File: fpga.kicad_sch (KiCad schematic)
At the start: 62 parts, among them IC4 XC3S250E-4VQG100C

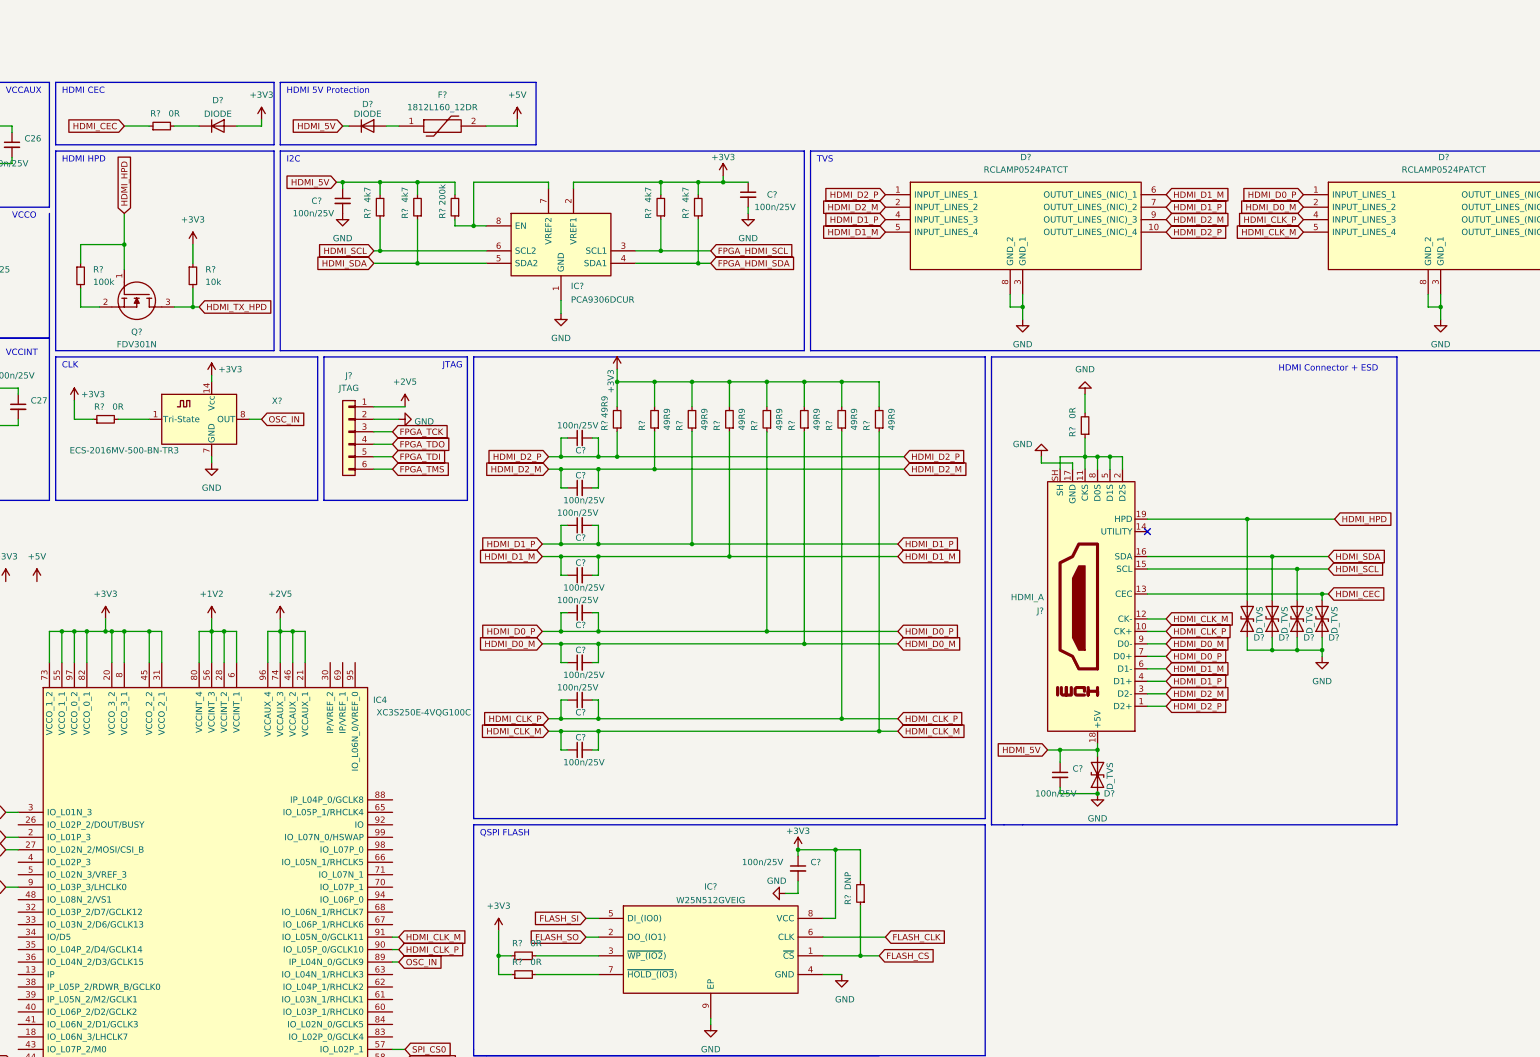
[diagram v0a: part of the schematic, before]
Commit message: update footprints for fpga
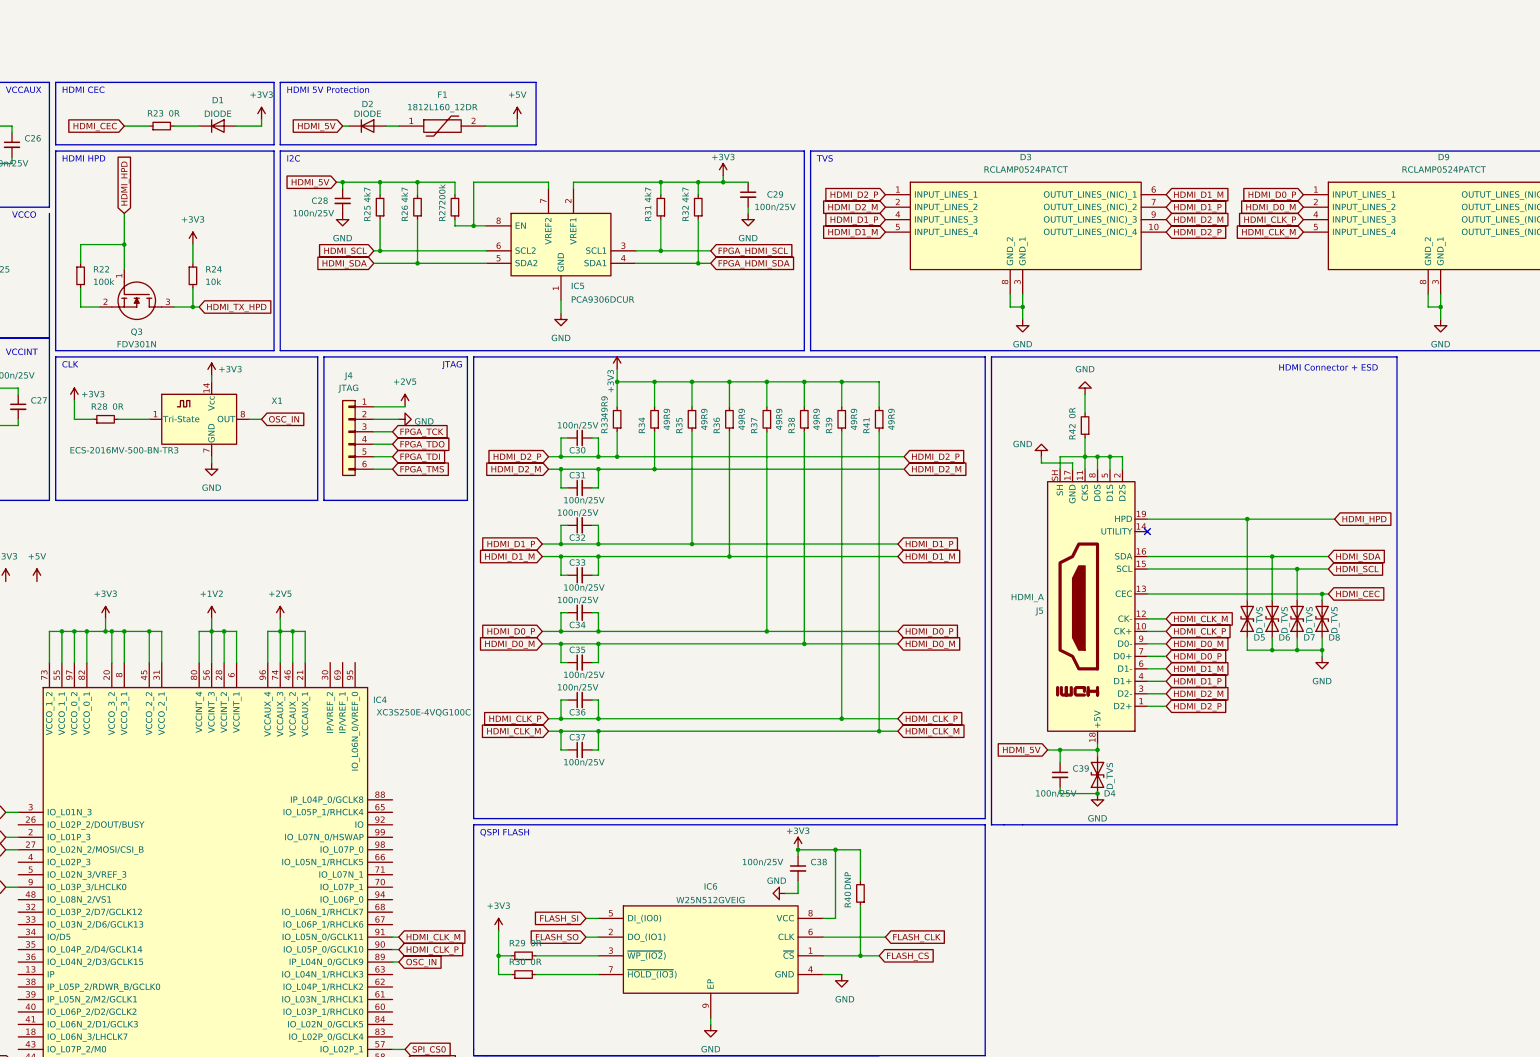
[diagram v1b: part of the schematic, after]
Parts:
- D3, D9: renamed from D?; footprint RCLAMP0524PATCT -> fpga:RCLAMP0524PATCT
- F1: renamed from F?; footprint 1812L010DR -> fpga:1812L010DR
- IC5: renamed from IC?; footprint SOP50P310X90-8N -> fpga:SOP50P310X90-8N
- J5: renamed from J?; footprint (none) -> SamacSys_Parts:HD0419THTR
- Q3: renamed from Q?; footprint SOT96P237X111-3N -> fpga:SOT96P237X111-3N
- gave numbers to parts that had none: 43

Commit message: Added FPGA footprints
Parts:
- D1: footprint (none) -> fpga:SODFL1608X70N
- D2: footprint (none) -> fpga:DIOM5126X265N
- J5: footprint SamacSys_Parts:HD0419THTR -> fpga:HD0419THTR
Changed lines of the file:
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@@
       (effects (font (size 1.27 1.27)) (justify left))
     )
-    (property "Footprint" "SamacSys_Parts:HD0419THTR" (id 2) (at 269.875 120.65 0)
+    (property "Footprint" "fpga:HD0419THTR" (id 2) (at 269.875 120.65 0)
       (effects (font (size 1.27 1.27)) hide)
     )
@@
     (property "Reference" "D2" (id 0) (at 121.92 18.415 0))
     (property "Value" "DIODE" (id 1) (at 121.92 20.3986 0))
-    (property "Footprint" "" (id 2) (at 121.92 22.86 0)
+    (property "Footprint" "fpga:DIOM5126X265N" (id 2) (at 121.92 22.86 0)
       (effects (font (size 1.27 1.27)) hide)
     )
@@
     (property "Reference" "D1" (id 0) (at 91.44 17.6235 0))
     (property "Value" "DIODE" (id 1) (at 91.44 20.3986 0))
-    (property "Footprint" "" (id 2) (at 91.44 22.86 0)
-      (effects (font (size 1.27 1.27)) hide)
-    )
+    (property "Footprint" "fpga:SODFL1608X70N" (id 2) (at 91.44 22.86 0)
+      (effects (font (size 1.27 1.27)) hide)
+    )
